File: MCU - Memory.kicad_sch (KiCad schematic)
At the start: 8 parts, among them IC1 W9864G6KH-6

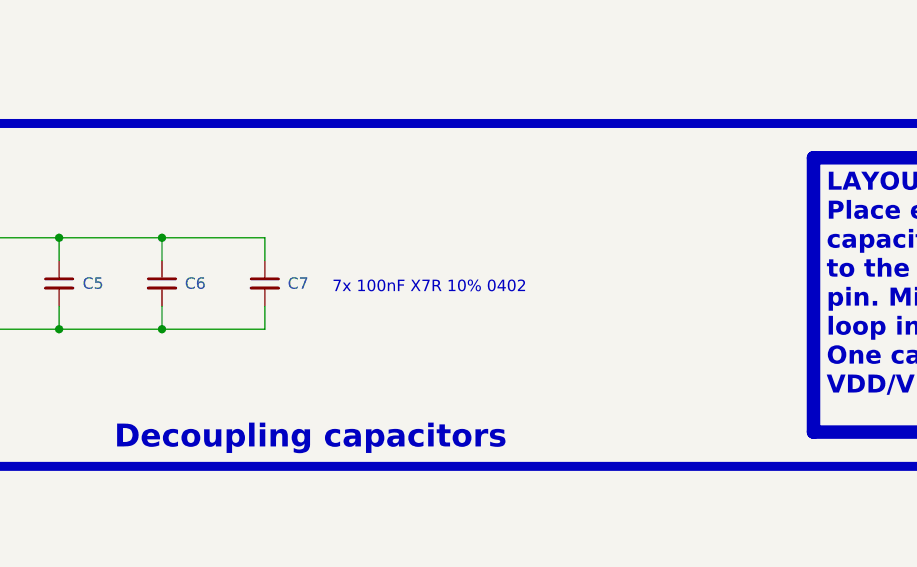
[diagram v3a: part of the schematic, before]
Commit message: added some small changes on schematics - added some decoupling caps and test production files
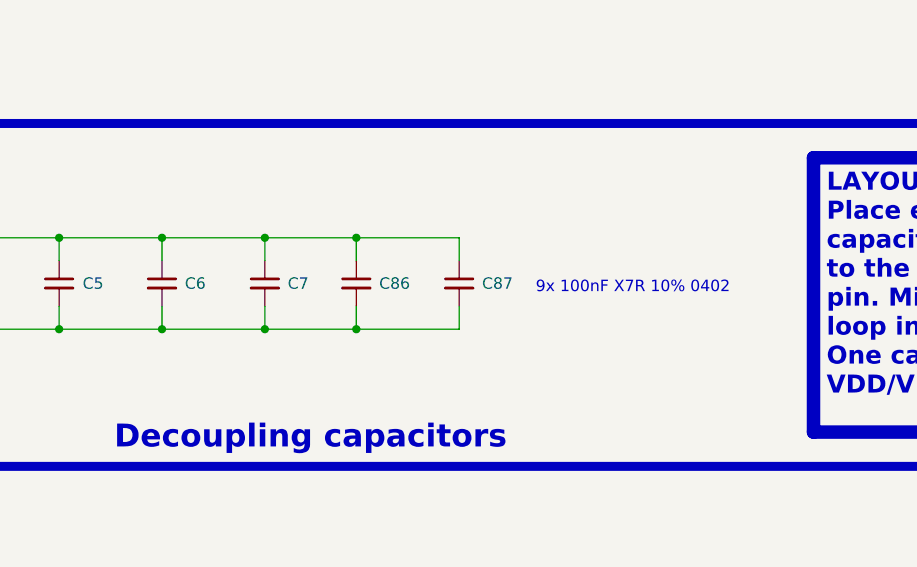
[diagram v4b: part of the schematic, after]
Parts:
- added C86, C87: 100nF, 0_capacitors:C_0402_1005Metric, symbol 0_capacitors:CL05B104KO5NNNC
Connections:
- net +3.3V: now also C86.1, C87.1
- net GND: now also C86.2, C87.2
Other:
- note added: "9x 100nF X7R 10% 0402"
- note removed: "7x 100nF X7R 10% 0402"
